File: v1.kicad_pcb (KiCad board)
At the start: 2 copper layers, 61 x 69.8 mm, 8 parts, among them J1 Screw_Terminal_01x04, U2 ESP32 DevKitV1 DoIt, U4 AHT20 Humidity Module

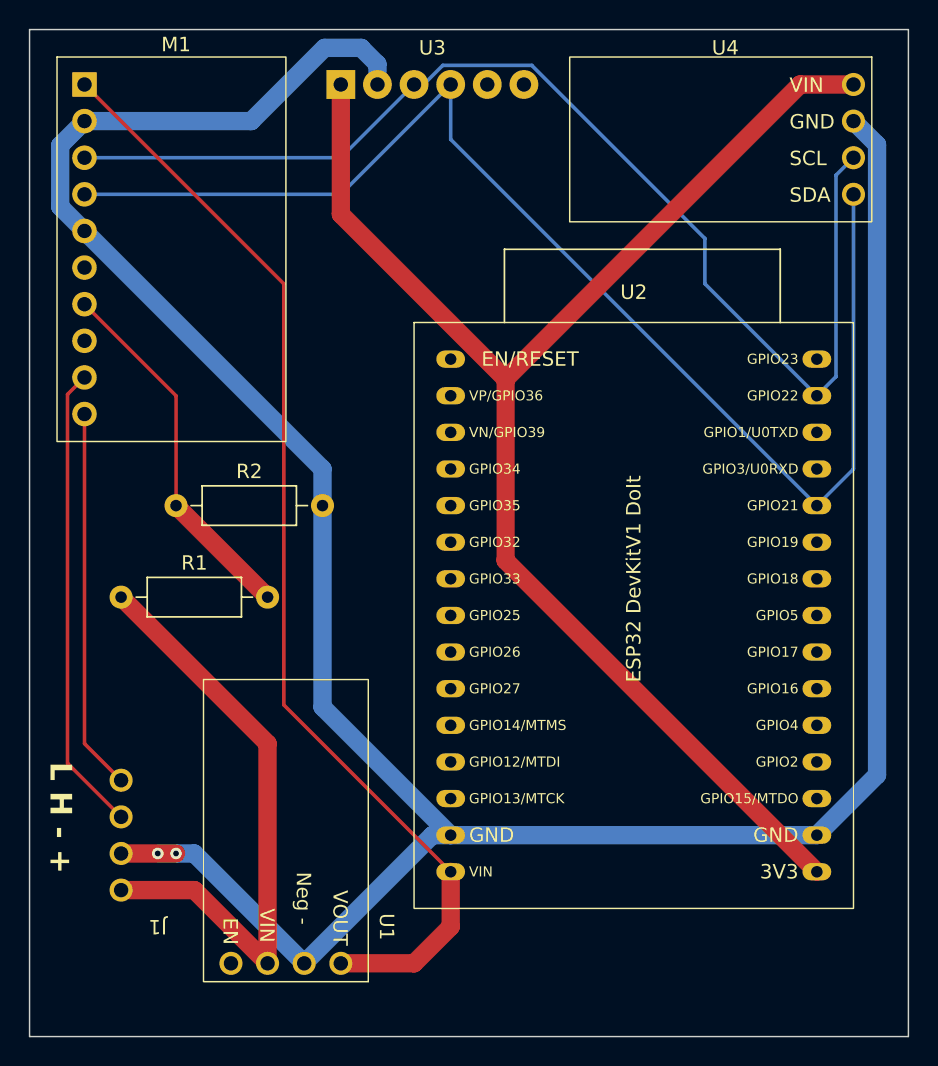
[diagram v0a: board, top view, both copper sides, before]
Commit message: Working on alternave voltage converter
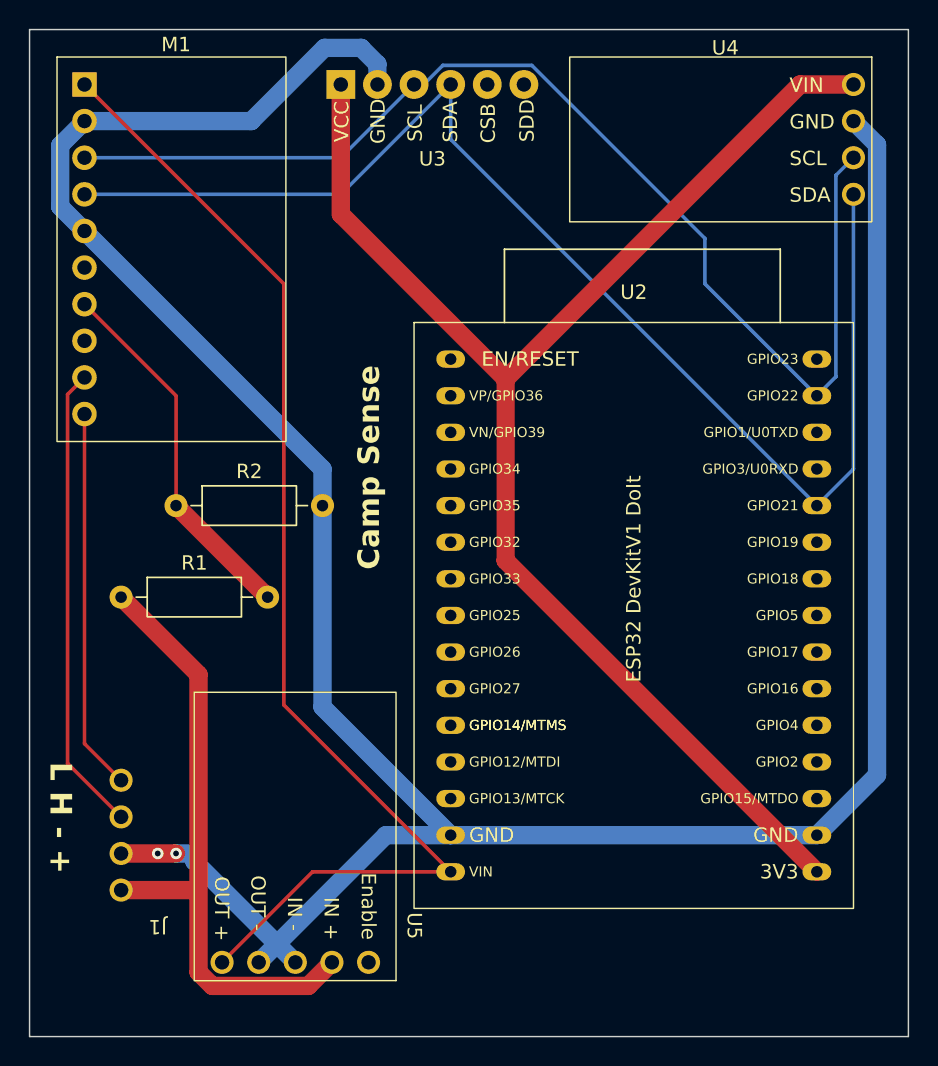
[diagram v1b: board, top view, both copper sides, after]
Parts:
- removed U1: ~, User:Drok Vreg
- added U5: ~, User:Drok Vreg_5pin, F.Cu at (152.0, 113.0)
- U4: value AHT20 Humidity Module -> AHT20
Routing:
- net +5V: track 77.6 -> 83.6 mm
- net GND: track 194.1 -> 196.9 mm
- net +12V: track 41.9 -> 43.6 mm
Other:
- board text added: "Camp Sense"
- board text added: "GPIO14/MTMS"

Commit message: Version 1.2 pcb, 3.3 volt adc, updated step down
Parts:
- R1: value 10000 -> 36000
- R2: value 5000 -> 10000
- U4: value AHT20 -> AHT20 Humidity Module
- renumbered U5 to U1
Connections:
- M1 pad 1: +5V -> +3V3
- U1 pad 5: +5V -> +3V3
- U2 pad 15: +5V -> unconnected-(U2-VIN-Pad15)
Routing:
- net +5V: track 83.6 -> 0.00 mm
- net +3V3: track 100.9 -> 162.8 mm
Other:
- board text added: "v1.2"
